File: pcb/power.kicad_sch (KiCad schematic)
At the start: 12 parts, among them J2 USB_C_Receptacle_USB2.0_14P, J3 Conn_01x02, J6 Conn_01x02, U2 nPM1300-QEXX

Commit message: Clean up sch
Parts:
- added C37: 2.2u, symbol Device:C
- C12: value 10u -> 1u
- R2: value 150k -> 255k
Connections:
- net +3V3: now also L2.1, U2.1 (VOUT1), U2.12 (VDDIO); no longer L2.2, U2.3 (SW1)
- net GND: now also C14.2, U2.18 (NTC), U2.28 (LSIN1/VINLDO1), U2.29 (LSOUT1/VOUTLDO1), U2.30 (LSIN2/VINLDO2), U2.31 (LSOUT2/VOUTLDO2), U2.33 (AVSS), U2.6 (PVSS2), C37.2
- net VBAT: now also C37.1
- net V_9151: now also U2.32 (VOUT2); no longer C12.1
- net at U2.22 (VBUSOUT): now also C12.1
- new net: L2.2, U2.3 (SW1)
- no-connect marks 0 -> 6
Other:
- note added: "Battery"
- note added: "Current Measurement"
- note added: "PMIC"
- note added: "PVDD - BUCK power in"
- note added: "PVSS1"
- note added: "See product spec section 9 for component selection"
- note added: "TODO: Find battery wtih thermistor"
- note added: "USB"
- note added: "VSYS - System voltage out"
- note removed: "BAT"
- note removed: "CHECK"
- note removed: "I MEAS"
- moved on the sheet: C10, C11, C13, C14, C9, J2, J3, J6, L2, R2, U2

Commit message: Footprints
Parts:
- C10, C11, C13: footprint (none) -> Capacitor_SMD:C_0805_2012Metric
- C12, C14, C37, C9, L2: footprint (none) -> Capacitor_SMD:C_0603_1608Metric
- J2: footprint (none) -> Connector_USB:USB_C_Receptacle_GCT_USB4105-xx-A_16P_TopMnt_Horizontal
- J3: footprint (none) -> Connector_JST:JST_SHL_SM02B-SHLS-TF_1x02-1MP_P1.00mm_Horizontal
- J6: footprint (none) -> Connector_PinHeader_2.54mm:PinHeader_1x02_P2.54mm_Vertical
- R2: footprint (none) -> Resistor_SMD:R_0603_1608Metric
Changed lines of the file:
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@@
-	(wire
-		(pts
-			(xy 248.92 105.41) (xy 248.92 111.76)
-		)
-		(stroke
-			(width 0)
-			(type default)
-		)
-	)
 	(wire
 		(pts
@@
 		(pts
 			(xy 121.92 123.19) (xy 124.46 123.19)
+		)
+		(stroke
+			(width 0)
+			(type default)
+		)
+	)
+	(wire
+		(pts
+			(xy 248.92 109.22) (xy 248.92 111.76)
 		)
 		(stroke
@@
 			)
 		)
-		(property "Footprint" ""
+		(property "Footprint" "Connector_PinHeader_2.54mm:PinHeader_1x02_P2.54mm_Vertical"
 			(at 233.68 43.18 0)
 			(effects
@@
 			)
 		)
-		(property "Footprint" ""
+		(property "Footprint" "Connector_JST:JST_SHL_SM02B-SHLS-TF_1x02-1MP_P1.00mm_Horizontal"
 			(at 233.68 50.8 0)
 			(effects
@@
 			)
 		)
-		(property "Footprint" ""
+		(property "Footprint" "Capacitor_SMD:C_0603_1608Metric"
 			(at 129.2352 153.67 0)
 			(effects
@@
 			)
 		)
-		(property "Footprint" ""
+		(property "Footprint" "Connector_USB:USB_C_Receptacle_GCT_USB4105-xx-A_16P_TopMnt_Horizontal"
 			(at 233.68 127 0)
 			(effects
@@
 			)
 		)
-		(property "Footprint" ""
+		(property "Footprint" "Capacitor_SMD:C_0603_1608Metric"
 			(at 133.0452 81.28 0)
 			(effects
@@
 			)
 		)
-		(property "Footprint" ""
+		(property "Footprint" "Capacitor_SMD:C_0805_2012Metric"
 			(at 144.4752 104.14 0)
 			(effects
@@
 			)
 		)
-		(property "Footprint" ""
+		(property "Footprint" "Capacitor_SMD:C_0603_1608Metric"
 			(at 133.35 99.06 0)
 			(effects
@@
 			)
 		)
-		(property "Footprint" ""
+		(property "Footprint" "Capacitor_SMD:C_0805_2012Metric"
 			(at 110.1852 68.58 0)
 			(effects
@@
 	(symbol
 		(lib_id "power:VBUS")
-		(at 248.92 105.41 0)
+		(at 248.92 109.22 0)
 		(unit 1)
 		(exclude_from_sim no)
@@
 		(fields_autoplaced yes)
 		(property "Reference" "#PWR014"
+			(at 248.92 113.03 0)
+			(effects
+				(font
+					(size 1.27 1.27)
+				)
+				(hide yes)
+			)
+		)
+		(property "Value" "VBUS"
+			(at 248.92 104.14 0)
+			(effects
+				(font
+					(size 1.27 1.27)
+				)
+			)
+		)
+		(property "Footprint" ""
 			(at 248.92 109.22 0)
 			(effects
@@
 			)
 		)
-		(property "Value" "VBUS"
-			(at 248.92 100.33 0)
-			(effects
-				(font
-					(size 1.27 1.27)
-				)
-			)
-		)
-		(property "Footprint" ""
-			(at 248.92 105.41 0)
-			(effects
-				(font
-					(size 1.27 1.27)
-				)
-				(hide yes)
-			)
-		)
 		(property "Datasheet" ""
-			(at 248.92 105.41 0)
+			(at 248.92 109.22 0)
 			(effects
 				(font
@@
 		)
 		(property "Description" "Power symbol creates a global label with name \"VBUS\""
-			(at 248.92 105.41 0)
+			(at 248.92 109.22 0)
 			(effects
 				(font
@@
 			)
 		)
-		(property "Footprint" ""
+		(property "Footprint" "Resistor_SMD:R_0603_1608Metric"
 			(at 35.052 143.51 90)
 			(effects
@@
 			)
 		)
-		(property "Footprint" ""
+		(property "Footprint" "Capacitor_SMD:C_0603_1608Metric"
 			(at 79.7052 68.58 0)
 			(effects
@@
 			)
 		)
-		(property "Footprint" ""
+		(property "Footprint" "Capacitor_SMD:C_0805_2012Metric"
 			(at 98.7552 68.58 0)
 			(effects
@@
 			)
 		)
-		(property "Footprint" ""
+		(property "Footprint" "Capacitor_SMD:C_0603_1608Metric"
 			(at 41.6052 90.17 0)
 			(effects

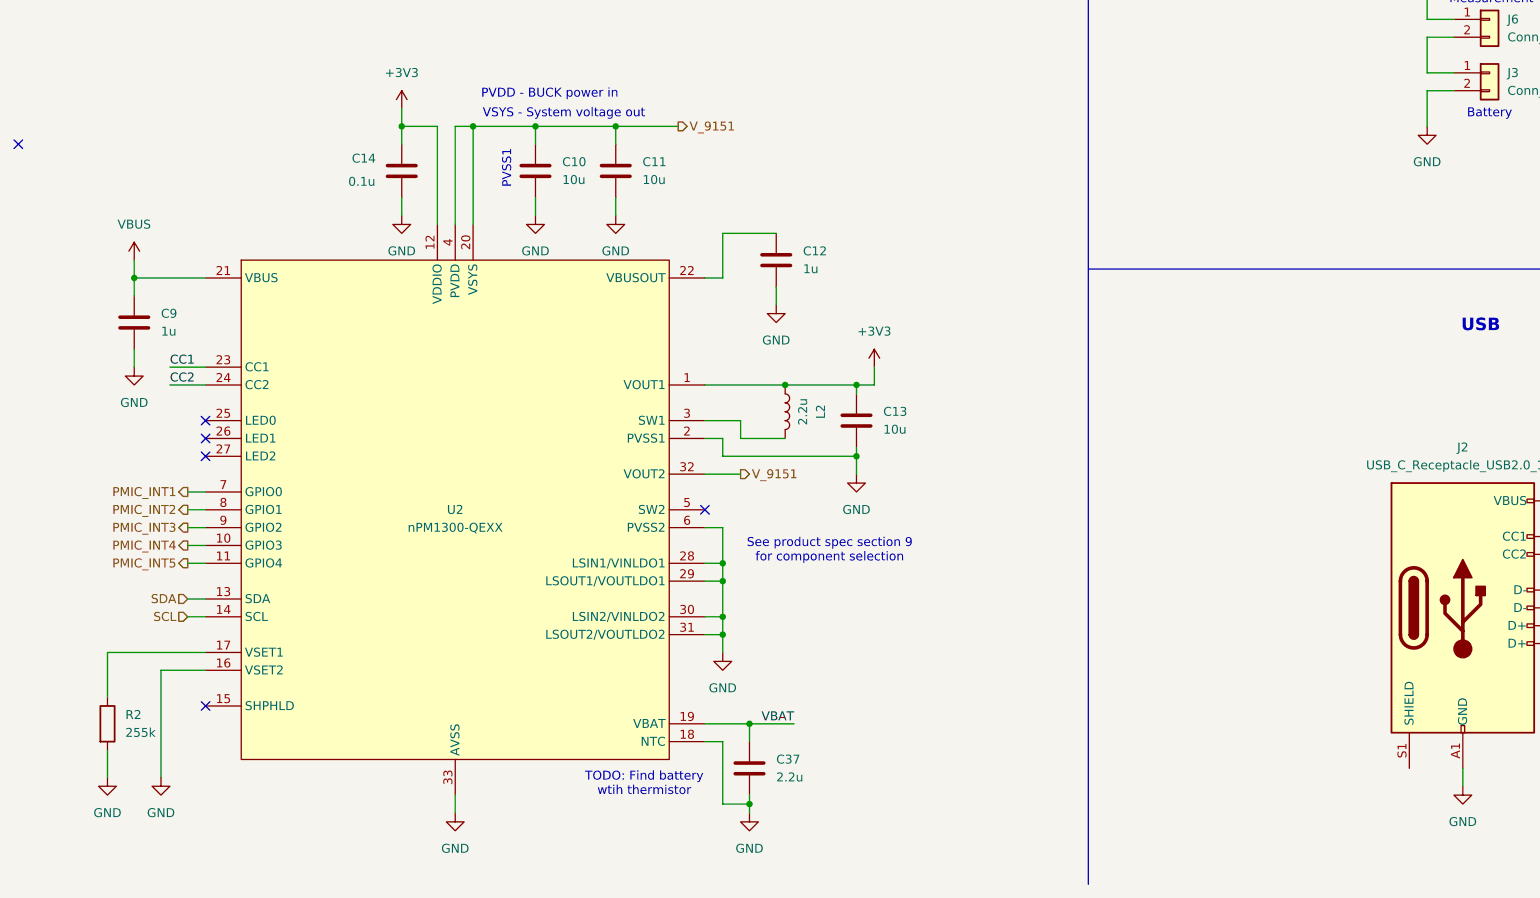
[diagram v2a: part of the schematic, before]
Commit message: ERC errors
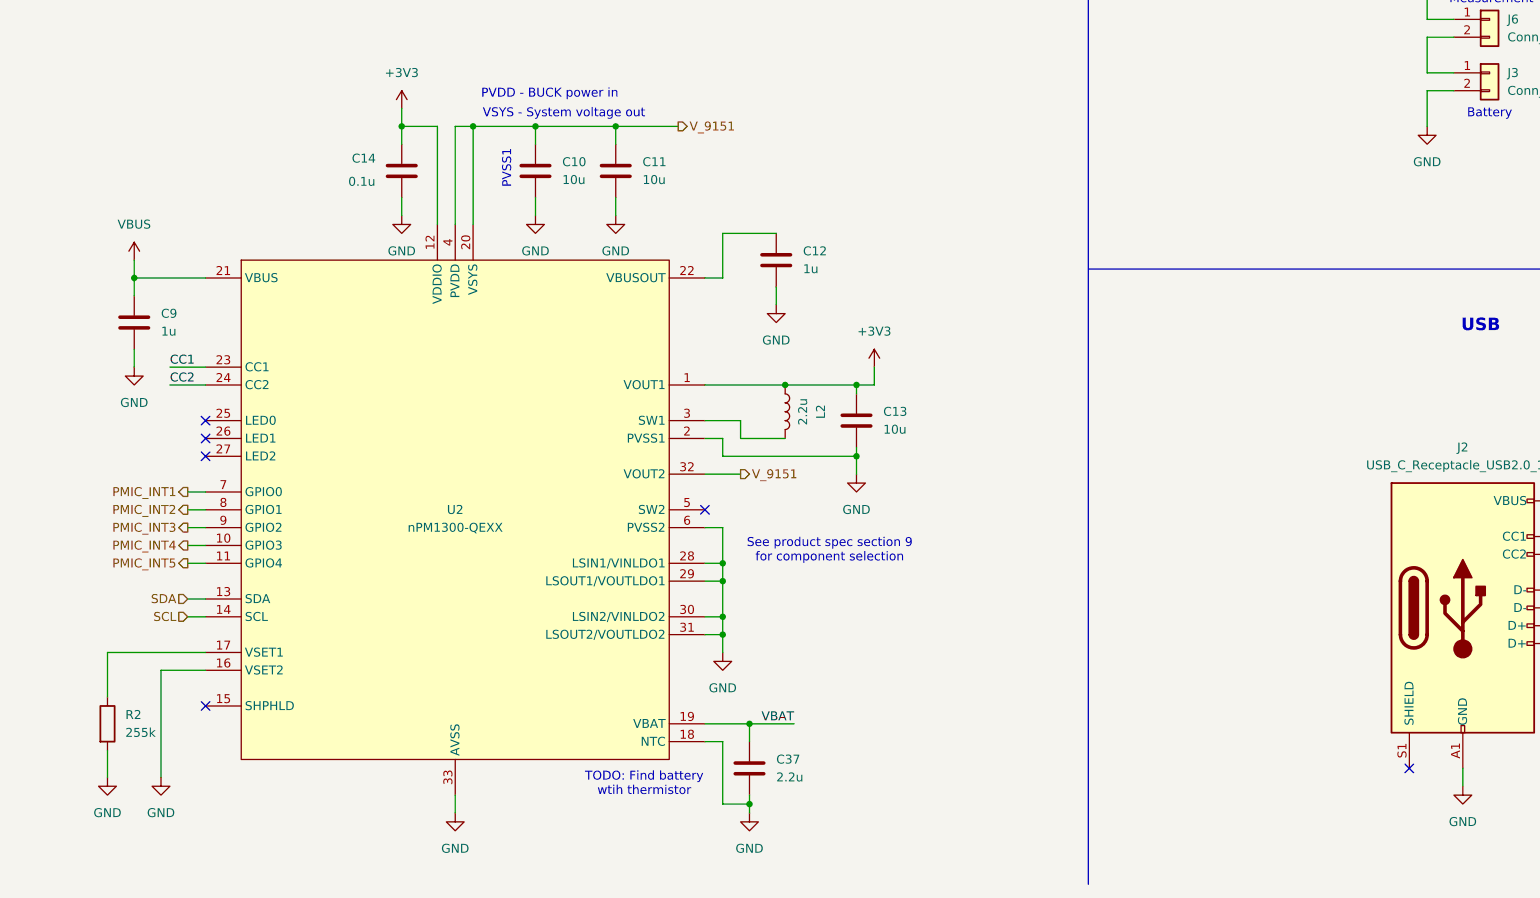
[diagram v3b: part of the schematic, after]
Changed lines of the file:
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@@
+	)
+	(junction
+		(at 88.9 58.42)
+		(diameter 0)
+		(color 0 0 0 0)
 	)
 	(junction
@@
 	)
 	(junction
-		(at 88.9 58.42)
-		(diameter 0)
-		(color 0 0 0 0)
-	)
-	(junction
 		(at 143.51 95.25)
 		(diameter 0)
@@
 	)
 	(no_connect
-		(at 24.13 60.96)
-	)
-	(no_connect
 		(at 50.8 140.97)
 	)
@@
 	)
 	(no_connect
+		(at 222.25 149.86)
+	)
+	(no_connect
 		(at 50.8 105.41)
 	)
 	(wire
 		(pts
-			(xy 97.79 58.42) (xy 88.9 58.42)
+			(xy 86.36 58.42) (xy 88.9 58.42)
 		)
 		(stroke
@@
 	(wire
 		(pts
+			(xy 88.9 58.42) (xy 88.9 72.39)
+		)
+		(stroke
+			(width 0)
+			(type default)
+		)
+	)
+	(wire
+		(pts
 			(xy 133.35 95.25) (xy 143.51 95.25)
 		)
@@
 	(wire
 		(pts
+			(xy 88.9 58.42) (xy 97.79 58.42)
+		)
+		(stroke
+			(width 0)
+			(type default)
+		)
+	)
+	(wire
+		(pts
 			(xy 45.72 92.71) (xy 50.8 92.71)
 		)
@@
 	(wire
 		(pts
-			(xy 88.9 58.42) (xy 88.9 72.39)
-		)
-		(stroke
-			(width 0)
-			(type default)
-		)
-	)
-	(wire
-		(pts
 			(xy 45.72 95.25) (xy 50.8 95.25)
 		)
@@
 		)
 		(stroke
-			(width 0)
-			(type default)
-		)
-	)
-	(wire
-		(pts
-			(xy 86.36 58.42) (xy 88.9 58.42)
-		)
-		(stroke

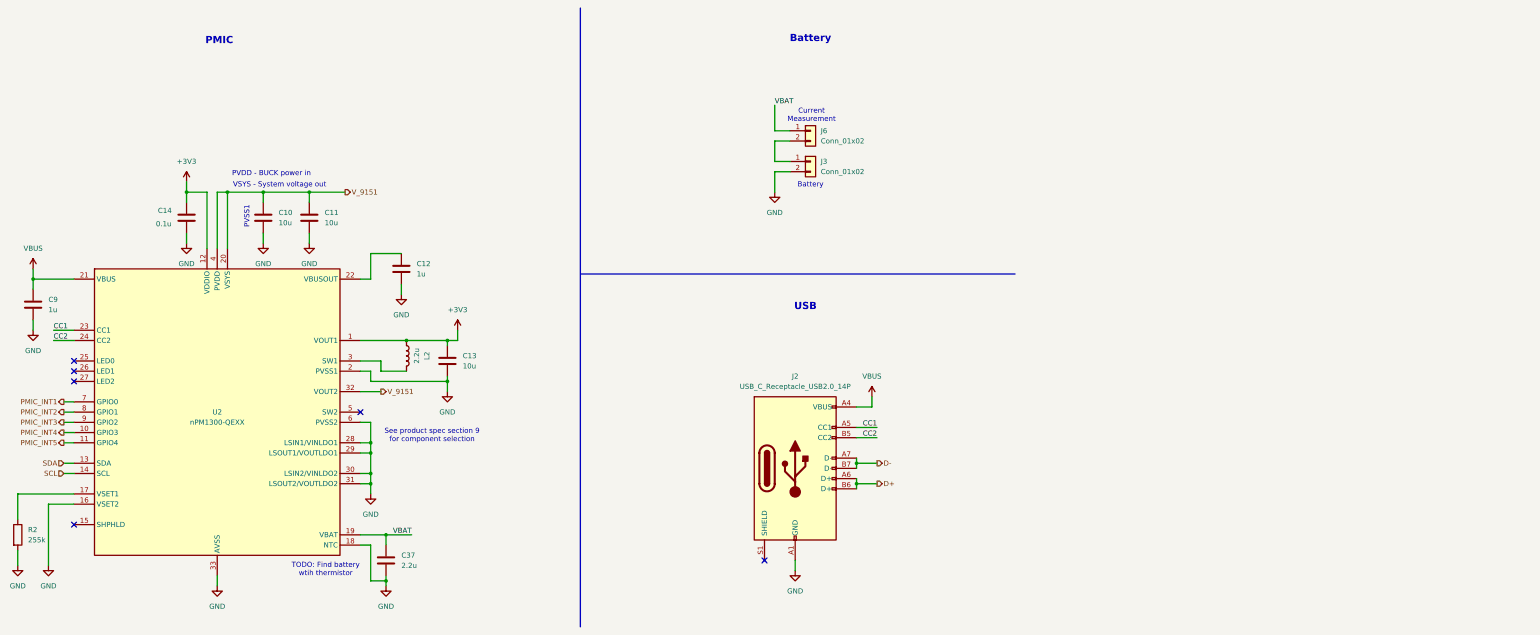
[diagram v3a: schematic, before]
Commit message: Add netclasses and usb-to-uart
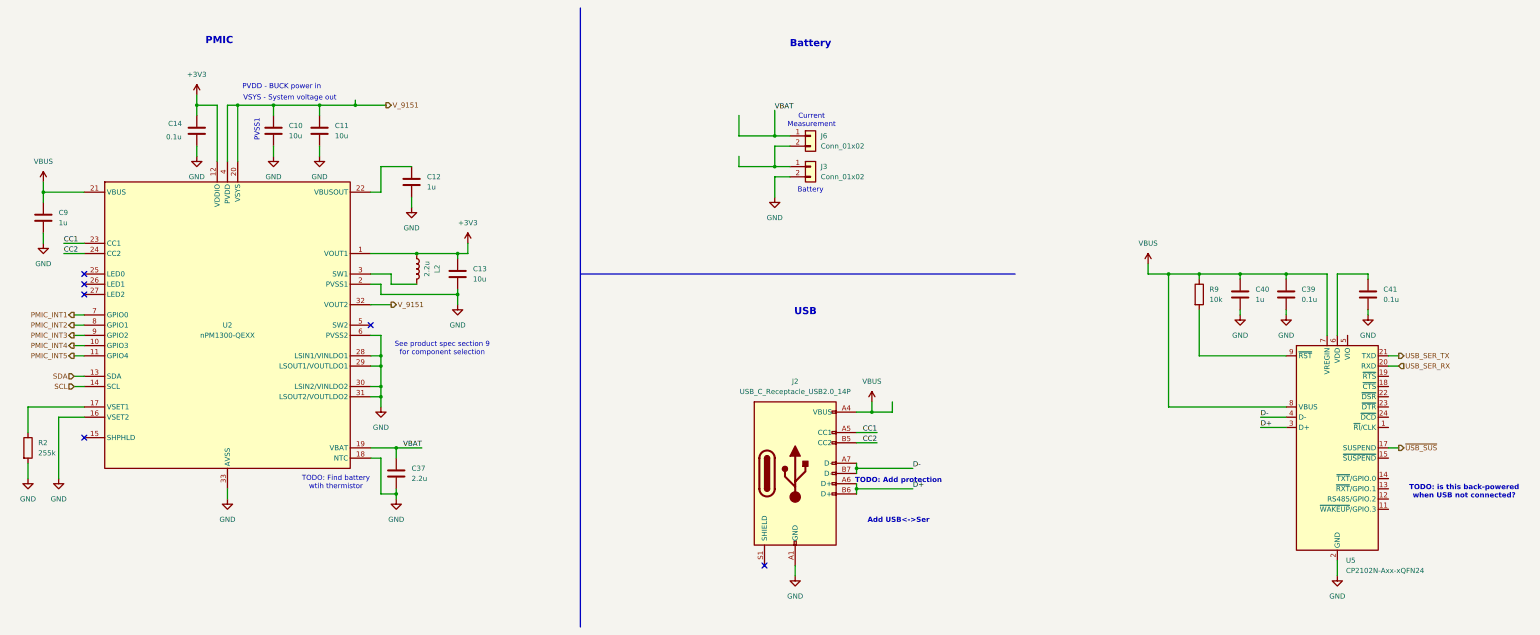
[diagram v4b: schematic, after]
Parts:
- added C39, C41: 0.1u, symbol Device:C
- added C40: 1u, symbol Device:C
- added R9: 10k, symbol Device:R
- added U5: CP2102N-Axx-xQFN24, Package_DFN_QFN:QFN-24-1EP_4x4mm_P0.5mm_EP2.6x2.6mm, symbol Interface_USB:CP2102N-Axx-xQFN24
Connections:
- net D+: now also U5.3 (D+)
- net D-: now also U5.4 (D-)
- net GND: now also C39.2, C40.2, C41.2, U5.2 (GND), U5.25 (GND)
- net VBUS: now also C39.1, C40.1, R9.1, U5.7 (VREGIN), U5.8 (VBUS)
- new net: C41.1, U5.6 (VDD)
- new net: R9.2, U5.9 (~{RST})
- new net USB_SER_RX: U5.20 (RXD)
- new net USB_SER_TX: U5.21 (TXD)
- new net ~{USB_SUS}: U5.17 (SUSPEND)
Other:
- note added: "Add USB<->Ser"
- note added: "TODO: Add protection"
- note added: "TODO: is this back-powered when USB not connected?"
- moved on the sheet: C10, C11, C12, C13, C14, C37, C9, J2, J3, J6, L2, R2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

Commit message: Adding filters
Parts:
- removed C39, C41: 0.1u, symbol Device:C
- removed C40: 1u, symbol Device:C
- removed J2: USB_C_Receptacle_USB2.0_14P, Connector_USB:USB_C_Receptacle_GCT_USB4105-xx-A_16P_TopMnt_Horizontal, symbol Connector:USB_C_Receptacle_USB2.0_14P
- removed J3: Conn_01x02, Connector_JST:JST_SHL_SM02B-SHLS-TF_1x02-1MP_P1.00mm_Horizontal, symbol Connector_Generic:Conn_01x02
- removed J6: Conn_01x02, Connector_PinHeader_2.54mm:PinHeader_1x02_P2.54mm_Vertical, symbol Connector_Generic:Conn_01x02
- removed R9: 10k, symbol Device:R
- removed U5: CP2102N-Axx-xQFN24, Package_DFN_QFN:QFN-24-1EP_4x4mm_P0.5mm_EP2.6x2.6mm, symbol Interface_USB:CP2102N-Axx-xQFN24
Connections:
- no-connect marks 6 -> 5
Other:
- note removed: "Add USB<->Ser"
- note removed: "Battery"
- note removed: "Current Measurement"
- note removed: "TODO: Add protection"
- note removed: "TODO: is this back-powered when USB not connected?"
- note removed: "USB"
- moved on the sheet: C10, C11, C12, C13, C14, C37, C9, L2, R2, U2

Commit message: Protection
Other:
- note removed: "See product spec section 9 for component selection"
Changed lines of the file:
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@@
-		)
-	)
-	(text "See product spec section 9 \nfor component selection"
-		(exclude_from_sim no)
-		(at 207.01 111.252 0)
-		(effects
-			(font
-				(size 1.27 1.27)
-				(color 255 0 248 1)
-			)
 		)
 	)
